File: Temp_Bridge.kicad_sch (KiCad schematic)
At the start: 4 parts

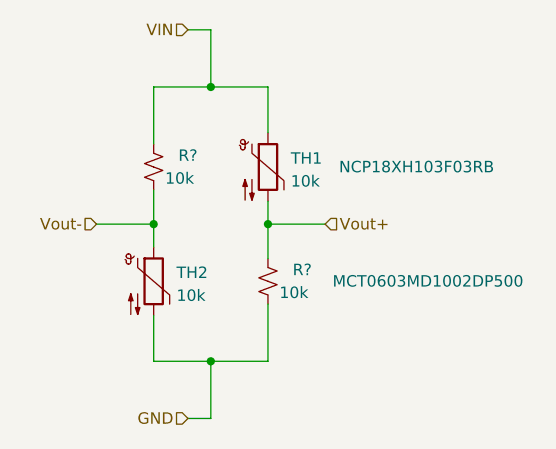
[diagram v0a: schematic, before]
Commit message: Updated Schematics with recent changes
Made Updates with recent suggestions.
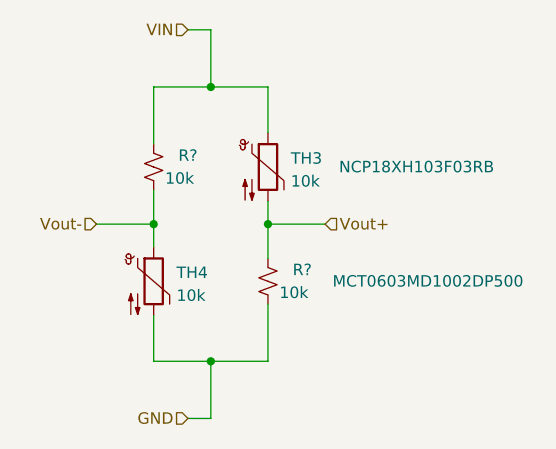
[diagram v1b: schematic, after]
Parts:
- renumbered TH1 to TH3, TH2 to TH4
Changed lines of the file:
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@@
         )
         (path "/674e1e7f-67ba-4e85-a926-dcd5f6a22021/db3c7ba2-982f-432b-8742-662861d58c3e/d7db0f74-5999-4270-8275-abfa9dfa973c"
-          (reference "R35") (unit 1)
+          (reference "R39") (unit 1)
         )
         (path "/674e1e7f-67ba-4e85-a926-dcd5f6a22021/db3c7ba2-982f-432b-8742-662861d58c3e/f7f024de-9e48-471e-a5a7-6e2bb622e9f9"
@@
         )
         (path "/674e1e7f-67ba-4e85-a926-dcd5f6a22021/db3c7ba2-982f-432b-8742-662861d58c3e/d1abd682-c78c-41d4-bc40-7db923db14b5"
-          (reference "R39") (unit 1)
-        )
-        (path "/674e1e7f-67ba-4e85-a926-dcd5f6a22021/db3c7ba2-982f-432b-8742-662861d58c3e/8f26b4a6-6006-4cb9-b746-b2201f266715"
           (reference "R41") (unit 1)
+        )
+        (path "/674e1e7f-67ba-4e85-a926-dcd5f6a22021/db3c7ba2-982f-432b-8742-662861d58c3e/8f26b4a6-6006-4cb9-b746-b2201f266715"
+          (reference "R46") (unit 1)
         )
       )
@@
   (symbol (lib_id "Device:Thermistor_NTC") (at 88.9 46.99 0) (unit 1)
     (in_bom yes) (on_board yes) (dnp no)
-    (property "Reference" "TH1" (at 91.44 46.0375 0)
+    (property "Reference" "TH3" (at 91.44 46.0375 0)
       (effects (font (size 1.27 1.27)) (justify left))
     )
@@
       (project "Quartz_v1p1"
         (path "/674e1e7f-67ba-4e85-a926-dcd5f6a22021/db3c7ba2-982f-432b-8742-662861d58c3e/d7db0f74-5999-4270-8275-abfa9dfa973c"
+          (reference "TH3") (unit 1)
+        )
+        (path "/674e1e7f-67ba-4e85-a926-dcd5f6a22021/db3c7ba2-982f-432b-8742-662861d58c3e/f7f024de-9e48-471e-a5a7-6e2bb622e9f9"
           (reference "TH1") (unit 1)
         )
-        (path "/674e1e7f-67ba-4e85-a926-dcd5f6a22021/db3c7ba2-982f-432b-8742-662861d58c3e/f7f024de-9e48-471e-a5a7-6e2bb622e9f9"
-          (reference "TH4") (unit 1)
-        )
-        (path "/674e1e7f-67ba-4e85-a926-dcd5f6a22021/db3c7ba2-982f-432b-8742-662861d58c3e/d1abd682-c78c-41d4-bc40-7db923db14b5"
-          (reference "TH6") (unit 1)
-        )
-        (path "/674e1e7f-67ba-4e85-a926-dcd5f6a22021/db3c7ba2-982f-432b-8742-662861d58c3e/8f26b4a6-6006-4cb9-b746-b2201f266715"
-          (reference "TH8") (unit 1)
+        (path "/674e1e7f-67ba-4e85-a926-dcd5f6a22021/db3c7ba2-982f-432b-8742-662861d58c3e/d1abd682-c78c-41d4-bc40-7db923db14b5"
+          (reference "TH5") (unit 1)
+        )
+        (path "/674e1e7f-67ba-4e85-a926-dcd5f6a22021/db3c7ba2-982f-432b-8742-662861d58c3e/8f26b4a6-6006-4cb9-b746-b2201f266715"
+          (reference "TH7") (unit 1)
         )
       )
@@
         )
         (path "/674e1e7f-67ba-4e85-a926-dcd5f6a22021/db3c7ba2-982f-432b-8742-662861d58c3e/d7db0f74-5999-4270-8275-abfa9dfa973c"
-          (reference "R36") (unit 1)
+          (reference "R40") (unit 1)
         )
         (path "/674e1e7f-67ba-4e85-a926-dcd5f6a22021/db3c7ba2-982f-432b-8742-662861d58c3e/f7f024de-9e48-471e-a5a7-6e2bb622e9f9"
@@
         )
         (path "/674e1e7f-67ba-4e85-a926-dcd5f6a22021/db3c7ba2-982f-432b-8742-662861d58c3e/d1abd682-c78c-41d4-bc40-7db923db14b5"
-          (reference "R40") (unit 1)
-        )
-        (path "/674e1e7f-67ba-4e85-a926-dcd5f6a22021/db3c7ba2-982f-432b-8742-662861d58c3e/8f26b4a6-6006-4cb9-b746-b2201f266715"
           (reference "R42") (unit 1)
+        )
+        (path "/674e1e7f-67ba-4e85-a926-dcd5f6a22021/db3c7ba2-982f-432b-8742-662861d58c3e/8f26b4a6-6006-4cb9-b746-b2201f266715"
+          (reference "R47") (unit 1)
         )
       )
@@
   (symbol (lib_id "Device:Thermistor_NTC") (at 76.2 59.69 0) (unit 1)
     (in_bom yes) (on_board yes) (dnp no) (fields_autoplaced)
-    (property "Reference" "TH2" (at 78.74 58.7375 0)
+    (property "Reference" "TH4" (at 78.74 58.7375 0)
       (effects (font (size 1.27 1.27)) (justify left))
     )
@@
       (project "Quartz_v1p1"
         (path "/674e1e7f-67ba-4e85-a926-dcd5f6a22021/db3c7ba2-982f-432b-8742-662861d58c3e/d7db0f74-5999-4270-8275-abfa9dfa973c"
+          (reference "TH4") (unit 1)
+        )
+        (path "/674e1e7f-67ba-4e85-a926-dcd5f6a22021/db3c7ba2-982f-432b-8742-662861d58c3e/f7f024de-9e48-471e-a5a7-6e2bb622e9f9"
           (reference "TH2") (unit 1)
         )
-        (path "/674e1e7f-67ba-4e85-a926-dcd5f6a22021/db3c7ba2-982f-432b-8742-662861d58c3e/f7f024de-9e48-471e-a5a7-6e2bb622e9f9"
-          (reference "TH3") (unit 1)
-        )
-        (path "/674e1e7f-67ba-4e85-a926-dcd5f6a22021/db3c7ba2-982f-432b-8742-662861d58c3e/d1abd682-c78c-41d4-bc40-7db923db14b5"
-          (reference "TH5") (unit 1)
-        )
-        (path "/674e1e7f-67ba-4e85-a926-dcd5f6a22021/db3c7ba2-982f-432b-8742-662861d58c3e/8f26b4a6-6006-4cb9-b746-b2201f266715"
-          (reference "TH7") (unit 1)
-        )
-      )
+        (path "/674e1e7f-67ba-4e85-a926-dcd5f6a22021/db3c7ba2-982f-432b-8742-662861d58c3e/d1abd682-c78c-41d4-bc40-7db923db14b5"
+          (reference "TH6") (unit 1)
+        )
+        (path "/674e1e7f-67ba-4e85-a926-dcd5f6a22021/db3c7ba2-982f-432b-8742-662861d58c3e/8f26b4a6-6006-4cb9-b746-b2201f266715"
+          (reference "TH8") (unit 1)
+        )
+      )
